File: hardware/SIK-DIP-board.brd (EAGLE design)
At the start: 96.5 x 66 mm, 76 parts

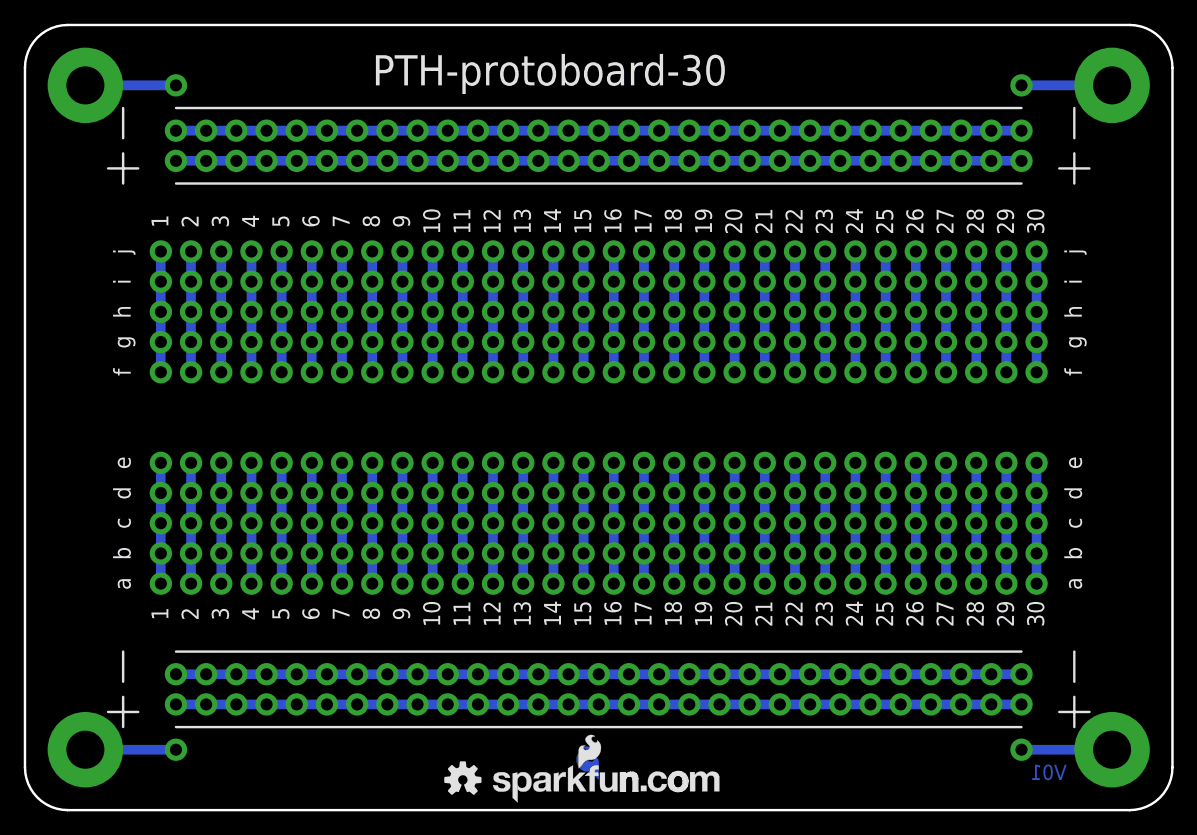
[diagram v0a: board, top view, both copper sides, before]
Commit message: Changed after reviewing prototype
Reversed text on bottom silk layer.
Shrunk overall dimension.
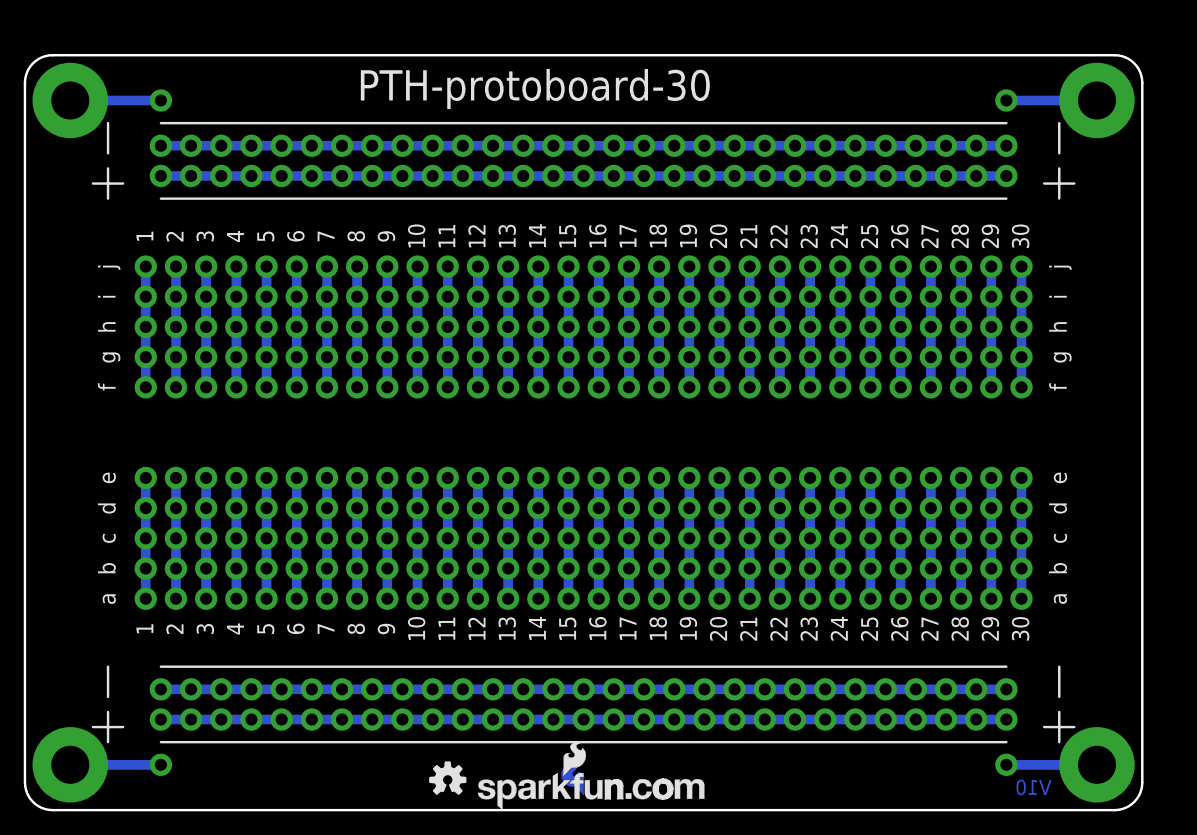
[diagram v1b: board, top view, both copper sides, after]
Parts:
- moved JP30 1.80 mm to (73.7, 17.8)
- moved JP32 1.80 mm to (78.7, 17.8)
- moved JP34 1.80 mm to (83.8, 17.8)
- moved JP60 1.80 mm to (73.7, 35.6)
- moved JP62 1.80 mm to (78.7, 35.6)
- moved JP64 1.80 mm to (83.8, 35.6)
- moved S1 1.80 mm to (3.81, 59.7)
- moved JP11 1.80 mm to (25.4, 17.8)
- moved JP18 1.80 mm to (43.2, 17.8)
- moved JP19 1.80 mm to (45.7, 17.8)
- moved JP20 1.80 mm to (48.3, 17.8)
- moved JP21 1.80 mm to (50.8, 17.8)
- moved JP66 1.80 mm to (11.4, 59.7)
- moved JP6 1.80 mm to (12.7, 17.8)
- moved JP7 1.80 mm to (15.2, 17.8)
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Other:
- board size 96.5 x 66 mm -> 94 x 63.5 mm
- board text added: "V10"
- board text removed: "V01"
